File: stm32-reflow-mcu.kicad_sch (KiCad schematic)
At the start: 22 parts, among them J1 TC2030, J2 Conn_01x04_Male, J3 Conn_01x03_Male, J4 Screw_Terminal_01x02, J5 Screw_Terminal_01x02, U1 STM32F051R4Tx, U2 MAX31855KASA, U3 MAX31855KASA, Y1 8MHz

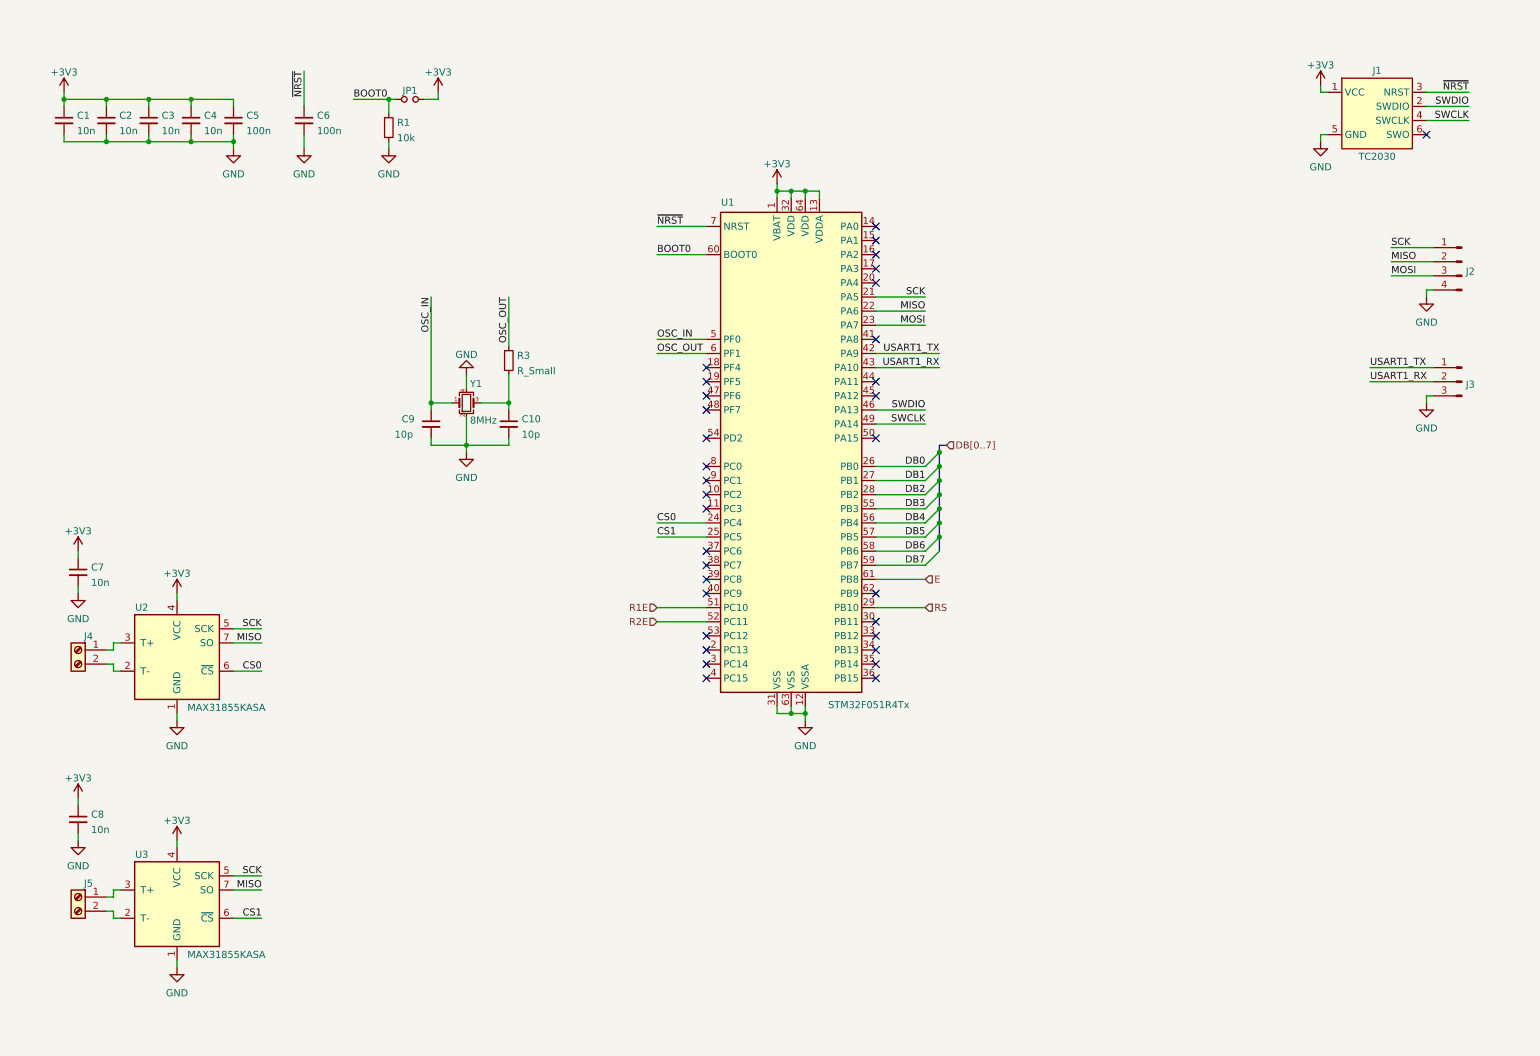
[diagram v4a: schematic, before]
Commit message: consolidated schematics for clarity, labeling and organization
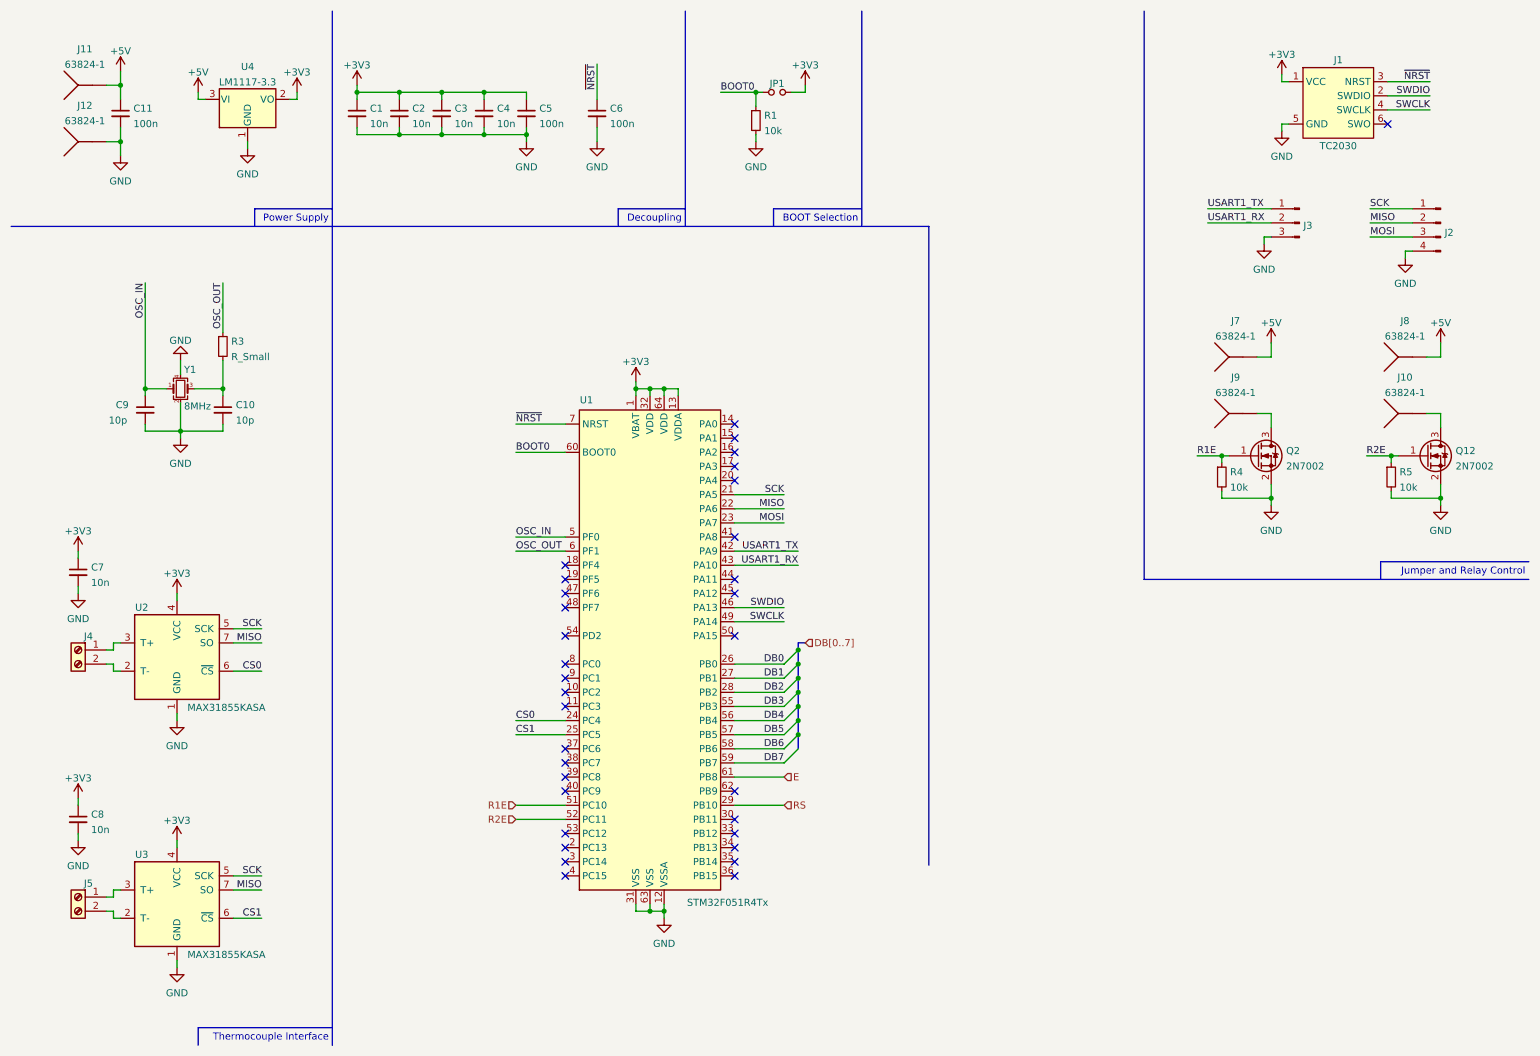
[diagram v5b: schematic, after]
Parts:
- added C11: 100n, Capacitor_SMD:C_0805_2012Metric, symbol Device:C_Small
- added J10, J11, J12, J7, J8, J9: 63824-1, Personal:CONN_63824-1, symbol Personal:63824-1
- added Q12, Q2: 2N7002, Package_TO_SOT_SMD:SOT-23, symbol Transistor_FET:2N7002
- added R4, R5: 10k, Resistor_SMD:R_0603_1608Metric, symbol Device:R_Small
- added U4: LM1117-3.3, Package_TO_SOT_SMD:SOT-223-3_TabPin2, symbol Regulator_Linear:LM1117-3.3
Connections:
- net +3V3: now also U4.2 (VO)
- net GND: now also C11.2, J12.1, J12.2, Q12.2 (S), Q2.2 (S), R4.2, R5.2, U4.1 (GND)
- net R1E: now also Q2.1 (G), R4.1
- net R2E: now also Q12.1 (G), R5.1
- new net: J9.1, J9.2, Q2.3 (D)
- new net: J10.1, J10.2, Q12.3 (D)
- new net +5V: C11.1, J11.1, J11.2, J7.1, J7.2, J8.1, J8.2, U4.3 (VI)
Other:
- note added: "BOOT Selection"
- note added: "Decoupling"
- note added: "Jumper and Relay Control"
- note added: "Power Supply"
- note added: "Thermocouple Interface"
- company: (none) -> de Byl Technologies, LLC
- title: (none) -> STM32 Reflow Controller
- moved on the sheet: C1, C10, C2, C3, C4, C5, C6, C9, J1, J2, J3, JP1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

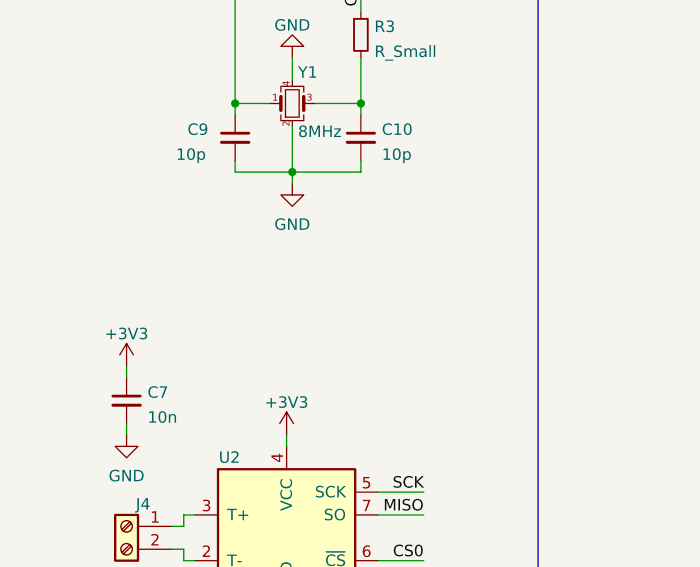
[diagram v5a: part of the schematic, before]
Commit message: added missign Oscillator schematic label
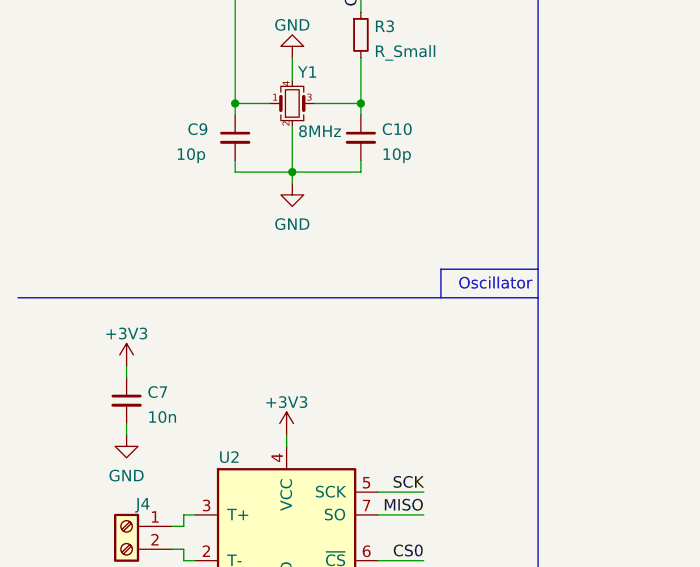
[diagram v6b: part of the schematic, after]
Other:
- note added: "Oscillator"
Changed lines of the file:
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@@
+    (stroke (width 0) (type default) (color 0 0 0 0))
+  )
+  (polyline (pts (xy 59.055 98.425) (xy 59.055 101.6))
     (stroke (width 0) (type default) (color 0 0 0 0))
   )
@@
   )
   (polyline (pts (xy 69.85 50.8) (xy 69.85 198.12))
+    (stroke (width 0) (type default) (color 0 0 0 0))
+  )
+  (polyline (pts (xy 69.85 98.425) (xy 59.055 98.425))
+    (stroke (width 0) (type default) (color 0 0 0 0))
+  )
+  (polyline (pts (xy 69.85 101.6) (xy 12.065 101.6))
     (stroke (width 0) (type default) (color 0 0 0 0))
   )
@@
     (effects (font (size 1.27 1.27)) (justify right bottom))
   )
+  (text "Oscillator" (at 69.215 100.965 180)
+    (effects (font (size 1.27 1.27)) (justify right bottom))
+  )
